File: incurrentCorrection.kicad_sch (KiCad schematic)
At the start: 5 parts, among them U6 LM358_DFN

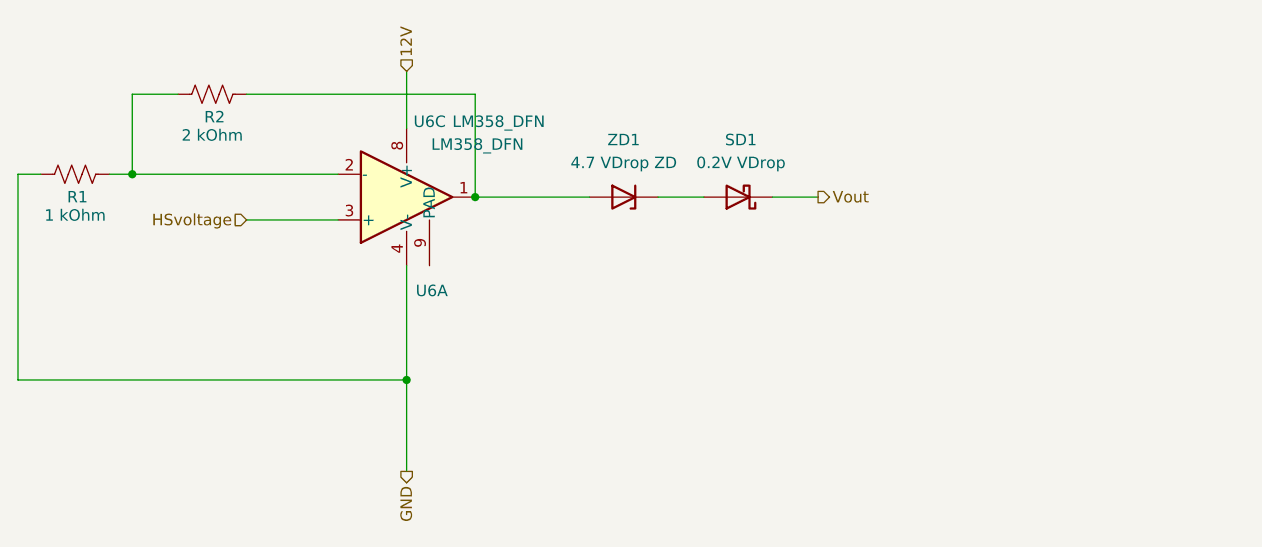
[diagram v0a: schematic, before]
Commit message: Schematic Complete
Completed the wiring of the circuit.

(Missing some labels and footprints)
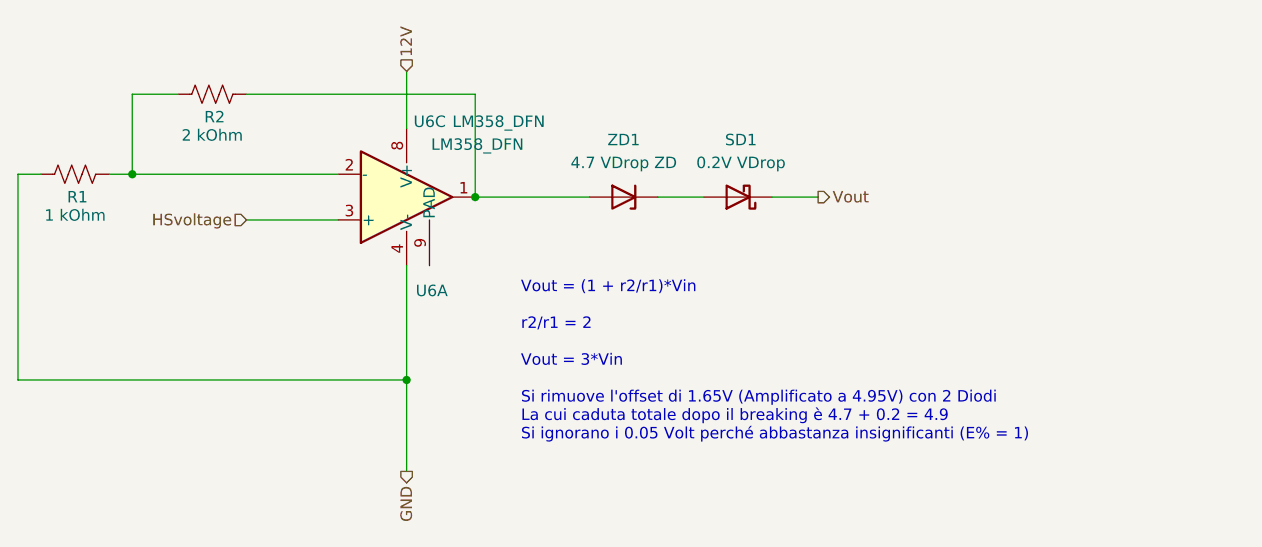
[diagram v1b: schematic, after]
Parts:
- R1: footprint (none) -> Resistor_SMD:R_1206_3216Metric_Pad1.30x1.75mm_HandSolder
- R2: footprint (none) -> Resistor_SMD:R_0402_1005Metric_Pad0.72x0.64mm_HandSolder
- SD1: footprint (none) -> Diode_SMD:Nexperia_DSN1608-2_1.6x0.8mm
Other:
- note added: "Vout = (1 + r2/r1)*Vin r2/r1 = 2 Vout = 3*Vin Si rimuove l'offset di 1.65V (Amplificato a 4.95V) con 2 Diodi La cui caduta totale dopo il breaking è 4.7 + 0.2 = 4.9 Si ignorano i 0.05 Volt perché abbastanza insignificanti (E% = 1)"
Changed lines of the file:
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@@
 	(generator_version "9.0")
 	(paper "A4")
+	(text "Vout = (1 + r2/r1)*Vin\n\nr2/r1 = 2\n\nVout = 3*Vin\n\nSi rimuove l'offset di 1.65V (Amplificato a 4.95V) con 2 Diodi\nLa cui caduta totale dopo il breaking è 4.7 + 0.2 = 4.9\nSi ignorano i 0.05 Volt perché abbastanza insignificanti (E% = 1)"
+		(exclude_from_sim no)
+		(at 157.48 86.868 0)
+		(effects
+			(font
+				(size 1.27 1.27)
+			)
+			(justify left)
+		)
+	)
 	(junction
 		(at 152.4 68.58)
@@
 			)
 		)
-		(property "Footprint" ""
+		(property "Footprint" "Diode_SMD:Nexperia_DSN1608-2_1.6x0.8mm"
 			(at 181.61 68.58 0)
 			(effects
@@
 			)
 		)
-		(property "Footprint" ""
+		(property "Footprint" "Resistor_SMD:R_1206_3216Metric_Pad1.30x1.75mm_HandSolder"
 			(at 108.204 65.024 90)
 			(effects
@@
 			)
 		)
-		(property "Footprint" ""
+		(property "Footprint" "Resistor_SMD:R_0402_1005Metric_Pad0.72x0.64mm_HandSolder"
 			(at 123.444 56.134 90)
 			(effects
